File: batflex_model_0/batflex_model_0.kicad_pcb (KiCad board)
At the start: 2 copper layers, 47.5 x 8 mm, 23 parts, among them J1 molex_505004, J2 molex_505006

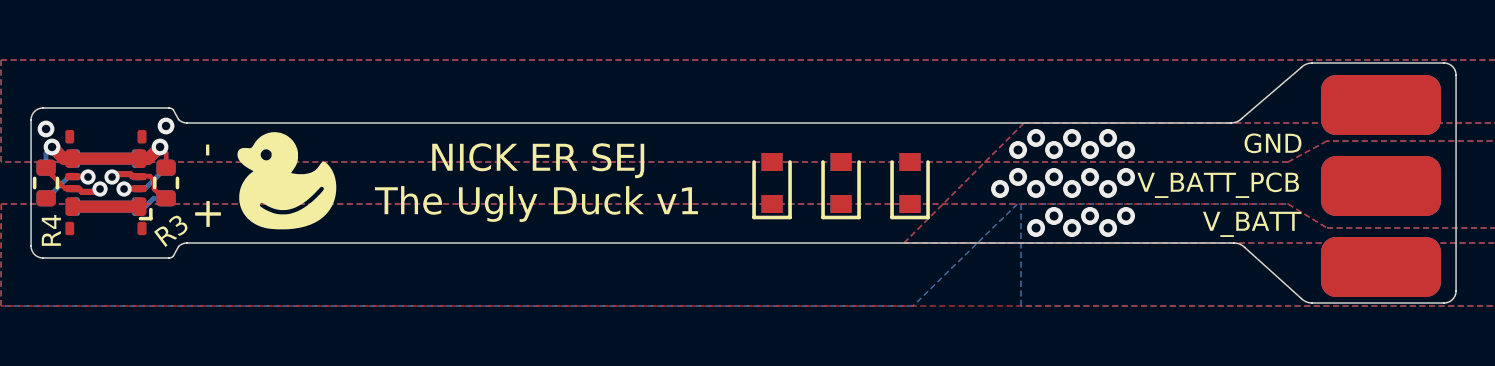
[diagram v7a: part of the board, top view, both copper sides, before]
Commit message: Final PCB for batflex model 0 aka the ugly duck
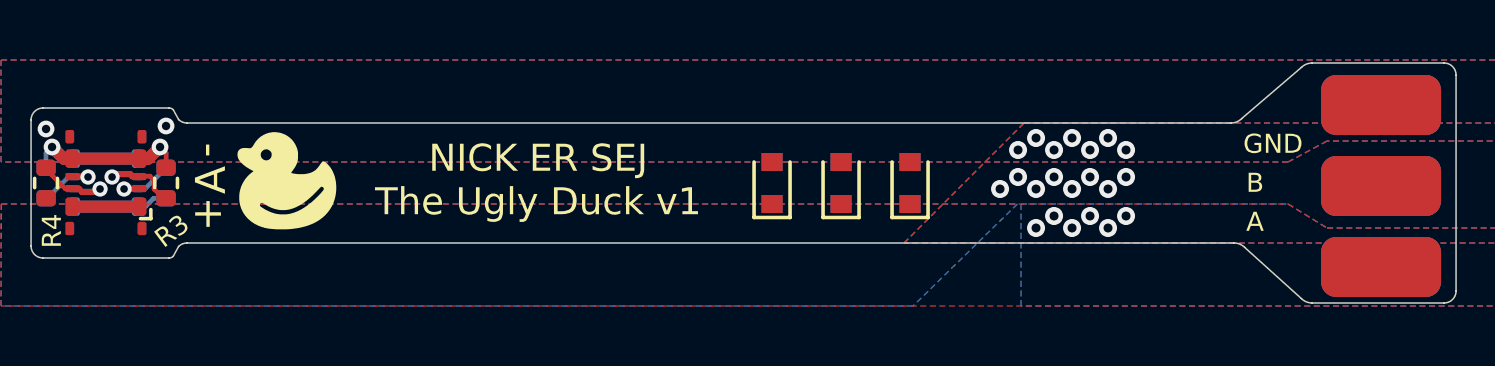
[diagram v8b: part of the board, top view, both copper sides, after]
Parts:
- TP2: value V_BATT_PCB -> B
- TP20: value V_BATT -> B
- TP3: value V_BATT -> A
- TP30: value V_BATT_PCB -> A
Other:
- board text added: "A"
- board text added: "B"
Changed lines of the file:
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@@
   (net 1 "/D")
   (net 2 "/C")
-  (net 3 "Net-(J1-Pad1)")
+  (net 3 "Net-(D101-Pad1)")
   (net 4 "/B")
   (net 5 "/A")
-  (net 6 "Net-(J2-Pad7)")
+  (net 6 "Net-(D102-Pad1)")
   (net 7 "/GND")
   (module "batflex:molex_5050040812" (layer "F.Cu")
@@
     (fp_line (start -1.25 2.1) (end 1.25 2.1) (layer "F.CrtYd") (width 0.05))
     (pad "1" smd roundrect (at -1.13 -0.8 270) (size 0.62 0.45) (layers "F.Cu" "F.Paste" "F.Mask") (roundrect_rratio 0.25)
-      (net 3 "Net-(J1-Pad1)") (pinfunction "Pin_1"))
+      (net 3 "Net-(D101-Pad1)") (pinfunction "Pin_1"))
     (pad "2" smd roundrect (at 1.13 -0.8 270) (size 0.62 0.45) (layers "F.Cu" "F.Paste" "F.Mask") (roundrect_rratio 0.25)
-      (net 3 "Net-(J1-Pad1)") (pinfunction "Pin_2"))
+      (net 3 "Net-(D101-Pad1)") (pinfunction "Pin_2"))
     (pad "3" smd roundrect (at -1.13 -0.2 270) (size 0.24 0.45) (layers "F.Cu" "F.Paste" "F.Mask") (roundrect_rratio 0.25)
       (net 4 "/B") (pinfunction "Pin_3"))
@@
     (fp_line (start -0.65 0.45) (end -0.65 -0.45) (layer "F.Fab") (width 0.1))
     (pad "1" smd rect (at -0.7 0 270) (size 0.6 0.7) (layers "F.Cu" "F.Paste" "F.Mask")
-      (net 3 "Net-(J1-Pad1)") (pinfunction "K") (zone_connect 2))
+      (net 3 "Net-(D101-Pad1)") (pinfunction "K") (zone_connect 2))
     (pad "2" smd rect (at 0.7 0 270) (size 0.6 0.7) (layers "F.Cu" "F.Paste" "F.Mask")
       (net 7 "/GND") (pinfunction "A") (zone_connect 2))
@@
     (fp_line (start -0.65 0.45) (end -0.65 -0.45) (layer "F.Fab") (width 0.1))
     (pad "1" smd rect (at -0.7 0 270) (size 0.6 0.7) (layers "F.Cu" "F.Paste" "F.Mask")
-      (net 3 "Net-(J1-Pad1)") (pinfunction "K") (zone_connect 2))
+      (net 3 "Net-(D101-Pad1)") (pinfunction "K") (zone_connect 2))
     (pad "2" smd rect (at 0.7 0 270) (size 0.6 0.7) (layers "F.Cu" "F.Paste" "F.Mask")
       (net 7 "/GND") (pinfunction "A") (zone_connect 2))
@@
     (fp_line (start -0.525 -0.27) (end 0.525 -0.27) (layer "F.Fab") (width 0.1))
     (pad "1" smd roundrect (at -0.51 0 90) (size 0.54 0.64) (layers "F.Cu" "F.Paste" "F.Mask") (roundrect_rratio 0.25)
-      (net 3 "Net-(J1-Pad1)"))
+      (net 3 "Net-(D101-Pad1)"))
     (pad "2" smd roundrect (at 0.51 0 90) (size 0.54 0.64) (layers "F.Cu" "F.Paste" "F.Mask") (roundrect_rratio 0.25)
       (net 1 "/D"))
@@
       (effects (font (size 0.635 0.635) (thickness 0.1524)))
     )
-    (fp_text value "V_BATT" (at 1.5 -4.3 180) (layer "F.SilkS")
+    (fp_text value "A" (at 1.5 -4.2 180) (layer "F.SilkS")
       (effects (font (size 0.635 0.635) (thickness 0.1524)))
     )
     (pad "1" smd roundrect (at 0 0 90) (size 2 4) (layers "F.Cu" "F.Paste" "F.Mask") (roundrect_rratio 0.25)
-      (net 3 "Net-(J1-Pad1)") (pinfunction "1") (zone_connect 2))
+      (net 3 "Net-(D101-Pad1)") (pinfunction "1") (zone_connect 2))
   )
   (module "Diode_SMD:D_SOD-523" (layer "F.Cu")
@@
     (fp_line (start 0.1 0.2) (end 0.1 -0.2) (layer "F.Fab") (width 0.1))
     (pad "1" smd rect (at -0.7 0 270) (size 0.6 0.7) (layers "F.Cu" "F.Paste" "F.Mask")
-      (net 3 "Net-(J1-Pad1)") (pinfunction "K") (zone_connect 2))
+      (net 3 "Net-(D101-Pad1)") (pinfunction "K") (zone_connect 2))
     (pad "2" smd rect (at 0.7 0 270) (size 0.6 0.7) (layers "F.Cu" "F.Paste" "F.Mask")
       (net 7 "/GND") (pinfunction "A") (zone_connect 2))
@@
       (effects (font (size 0.635 0.635) (thickness 0.1524)))
     )
-    (fp_text value "V_BATT_PCB" (at 0.1 -5.4 180) (layer "F.SilkS")
+    (fp_text value "B" (at 0.1 -4.2 180) (layer "F.SilkS")
       (effects (font (size 0.635 0.635) (thickness 0.1524)))
     )
     (pad "1" smd roundrect (at 0 0 90) (size 2 4) (layers "F.Cu" "F.Paste" "F.Mask") (roundrect_rratio 0.25)
-      (net 6 "Net-(J2-Pad7)") (pinfunction "1") (zone_connect 2))
+      (net 6 "Net-(D102-Pad1)") (pinfunction "1") (zone_connect 2))
   )
   (module "LOGO" locked (layer "B.Cu")
@@
     (fp_line (start -0.525 0.27) (end 0.525 0.27) (layer "B.Fab") (width 0.1))
     (pad "1" smd roundrect (at -0.51 0 90) (size 0.54 0.64) (layers "B.Cu" "B.Paste" "B.Mask") (roundrect_rratio 0.25)
-      (net 6 "Net-(J2-Pad7)"))
+      (net 6 "Net-(D102-Pad1)"))
     (pad "2" smd roundrect (at 0.51 0 90) (size 0.54 0.64) (layers "B.Cu" "B.Paste" "B.Mask") (roundrect_rratio 0.25)
       (net 4 "/B"))
@@
       (effects (font (size 0.635 0.635) (thickness 0.1524)) (justify mirror))
     )
-    (fp_text value "V_BATT" (at -0.099999 4.3 180) (layer "B.SilkS")
+    (fp_text value "B" (at -0.099999 4.2 180) (layer "B.SilkS")
       (effects (font (size 0.635 0.635) (thickness 0.1524)) (justify mirror))
     )
     (pad "1" smd roundrect (at 0 0 270) (size 2 4) (layers "B.Cu" "B.Paste" "B.Mask") (roundrect_rratio 0.25)
-      (net 6 "Net-(J2-Pad7)") (pinfunction "1") (zone_connect 2))
+      (net 6 "Net-(D102-Pad1)") (pinfunction "1") (zone_connect 2))
   )
   (module "batflex:wire_pad_2x4mm" (layer "B.Cu")
@@
       (effects (font (size 0.635 0.635) (thickness 0.1524)) (justify mirror))
     )
-    (fp_text value "V_BATT_PCB" (at -1.5 5.5 180) (layer "B.SilkS")
+    (fp_text value "A" (at -1.500001 4.2 180) (layer "B.SilkS")
       (effects (font (size 0.635 0.635) (thickness 0.1524)) (justify mirror))
     )
     (pad "1" smd roundrect (at 0 0 270) (size 2 4) (layers "B.Cu" "B.Paste" "B.Mask") (roundrect_rratio 0.25)
-      (net 3 "Net-(J1-Pad1)") (pinfunction "1") (zone_connect 2))
+      (net 3 "Net-(D101-Pad1)") (pinfunction "1") (zone_connect 2))
   )
   (module "Diode_SMD:D_SOD-523" (layer "B.Cu")
@@
     (fp_line (start 0.1 0) (end 0.25 0) (layer "B.Fab") (width 0.1))
     (pad "1" smd rect (at -0.7 0 270) (size 0.6 0.7) (layers "B.Cu" "B.Paste" "B.Mask")
-      (net 6 "Net-(J2-Pad7)") (pinfunction "K") (zone_connect 2))
+      (net 6 "Net-(D102-Pad1)") (pinfunction "K") (zone_connect 2))
     (pad "2" smd rect (at 0.7 0 270) (size 0.6 0.7) (layers "B.Cu" "B.Paste" "B.Mask")
       (net 7 "/GND") (pinfunction "A") (zone_connect 2))
@@
       (net 1 "/D") (pinfunction "Pin_6"))
     (pad "7" smd roundrect (at -1.05 -0.8 90) (size 0.62 0.38) (layers "B.Cu" "B.Paste" "B.Mask") (roundrect_rratio 0.25)
-      (net 6 "Net-(J2-Pad7)") (pinfunction "Pin_7"))
+      (net 6 "Net-(D102-Pad1)") (pinfunction "Pin_7"))
     (pad "8" smd roundrect (at 1.05 -0.8 90) (size 0.62 0.38) (layers "B.Cu" "B.Paste" "B.Mask") (roundrect_rratio 0.25)
-      (net 6 "Net-(J2-Pad7)") (pinfunction "Pin_8"))
+      (net 6 "Net-(D102-Pad1)") (pinfunction "Pin_8"))
     (model "${KIPRJMOD}/../3d/5050060812.stp"
       (offset (xyz 0 0 0))
@@
     (fp_line (start -0.65 -0.45) (end -0.65 0.45) (layer "B.Fab") (width 0.1))
     (pad "1" smd rect (at -0.7 0 270) (size 0.6 0.7) (layers "B.Cu" "B.Paste" "B.Mask")
-      (net 6 "Net-(J2-Pad7)") (pinfunction "K") (zone_connect 2))
+      (net 6 "Net-(D102-Pad1)") (pinfunction "K") (zone_connect 2))
     (pad "2" smd rect (at 0.7 0 270) (size 0.6 0.7) (layers "B.Cu" "B.Paste" "B.Mask")
       (net 7 "/GND") (pinfunction "A") (zone_connect 2))
@@
     (fp_line (start 0.1 0) (end 0.25 0) (layer "B.Fab") (width 0.1))
     (pad "1" smd rect (at -0.7 0 270) (size 0.6 0.7) (layers "B.Cu" "B.Paste" "B.Mask")
-      (net 6 "Net-(J2-Pad7)") (pinfunction "K") (zone_connect 2))
+      (net 6 "Net-(D102-Pad1)") (pinfunction "K") (zone_connect 2))
     (pad "2" smd rect (at 0.7 0 270) (size 0.6 0.7) (layers "B.Cu" "B.Paste" "B.Mask")
       (net 7 "/GND") (pinfunction "A") (zone_connect 2))
@@
   (gr_arc (start 194.3 103.6) (end 194.3 104) (angle -90) (layer "Edge.Cuts") (width 0.05))
   (gr_line (start 189.9 104) (end 194.3 104) (layer "Edge.Cuts") (width 0.05))
+  (gr_text "B" (at 153.2 99.9 90) (layer "B.SilkS")
+    (effects (font (size 1 1) (thickness 0.15)) (justify mirror))
+  )
   (gr_text "-" (at 153 98.9 90) (layer "B.SilkS")
     (effects (font (size 1 1) (thickness 0.15)))
@@
     (effects (font (size 1 1) (thickness 0.15)))
   )
+  (gr_text "A" (at 153.2 99.9 90) (layer "F.SilkS")
+    (effects (font (size 1 1) (thickness 0.15)))
+  )
   (gr_text "+" (at 153.1 101) (layer "F.SilkS")
     (effects (font (size 1 1) (thickness 0.15)))
@@
     )
   )
-  (zone (net 6) (net_name "Net-(J2-Pad7)") (layers F&B.Cu) (hatch edge 0.508)
+  (zone (net 6) (net_name "Net-(D102-Pad1)") (layers F&B.Cu) (hatch edge 0.508)
     (connect_pads (clearance 0.15))
     (min_thickness 0.254) (filled_areas_thickness no)
@@
     )
   )
-  (zone (net 3) (net_name "Net-(J1-Pad1)") (layer "F.Cu") (hatch edge 0.508)
+  (zone (net 3) (net_name "Net-(D101-Pad1)") (layer "F.Cu") (hatch edge 0.508)
     (priority 1)
     (connect_pads (clearance 0.15))
@@
     )
   )
-  (zone (net 3) (net_name "Net-(J1-Pad1)") (layer "B.Cu") (hatch edge 0.508)
+  (zone (net 3) (net_name "Net-(D101-Pad1)") (layer "B.Cu") (hatch edge 0.508)
     (priority 1)
     (connect_pads (clearance 0.15))
@@
     )
   )
-  (zone (net 6) (net_name "Net-(J2-Pad7)") (layer "B.Cu") (hatch edge 0.508)
+  (zone (net 6) (net_name "Net-(D102-Pad1)") (layer "B.Cu") (hatch edge 0.508)
     (priority 1)
     (connect_pads (clearance 0.15))
